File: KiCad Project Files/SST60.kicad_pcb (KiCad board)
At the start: 2 copper layers, 284.7 x 94.2 mm, 203 parts, among them J1 SM04B, J2 SWD, SW1 Boot, SW2 Reset, U1 RP2040, U2 W25Q128JVS, U3 XC6206PxxxMR, U4 PRTR5V0U2X, U5 74AHCT1G125, Y1 12MHz

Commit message: Cleaned Traces
Updated traces, generated new gerber, pos and bom, removed iso enter support
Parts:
- removed 3u Split: MX-NoLED, MX_Alps_Hybrid:MX-3U-ReversedStabilizers-NoLED (x2)
- removed D24, D29, D47, D60: D_Small, Diode_SMD:D_SOD-123
- removed the ISO at (284.2, 87.3)
- removed the ISO at (305.6, 77.8)
- removed MX77: MX-NoLED, MX_Alps_Hybrid:MX-10U-ReversedStabilizers-NoLED
- removed the Small Split at (117.5, 125.4)
- removed the Small Split at (148.4, 125.4)
- removed the Small Split at (196.1, 125.4)
- added 1.25U: MX-NoLED, MX_Alps_Hybrid:MX-1.25U-NoLED, F.Cu at (67.6, 125.5)
- added 1.25U: MX-NoLED, MX_Alps_Hybrid:MX-1.25U-NoLED, F.Cu at (91.5, 125.5)
- added 1.25U: MX-NoLED, MX_Alps_Hybrid:MX-1.25U-NoLED, F.Cu at (234.2, 125.4)
- added 1.25U: MX-NoLED, MX_Alps_Hybrid:MX-1.25U-NoLED, F.Cu at (305.7, 125.4)
- added 1.25U: MX-NoLED, MX_Alps_Hybrid:MX-1.25U-NoLED, F.Cu at (281.8, 125.4)
- added 1.25U: MX-NoLED, MX_Alps_Hybrid:MX-1.25U-NoLED, F.Cu at (43.8, 125.3)
- added 1.25U: MX-NoLED, MX_Alps_Hybrid:MX-1.25U-NoLED, F.Cu at (258.0, 125.5)
- added 2: MX-NoLED, MX_Alps_Hybrid:MX-1U-NoLED, F.Cu at (60.4, 49.2)
- added 2: MX-NoLED, MX_Alps_Hybrid:MX-1U-NoLED, F.Cu at (160.3, 106.4)
- added REF**: SW_Cherry_MX_6.25u_PCB, Button_Switch_Keyboard:SW_Cherry_MX_6.25u_PCB, F.Cu at (160.4, 130.5)
- moved D52 18.7 mm to (216.2, 127.1)
- moved D62 11.7 mm to (294.1, 128.6)
- moved D57 6.92 mm to (265.6, 127.1)
- moved D76 6.81 mm to (152.8, 119.8)
- moved D15 6.59 mm to (101.2, 122.3), turned to 180 degrees
- moved D38 5.39 mm to (183.1, 127.1)
- moved D10 4.61 mm to (77.6, 127.1)
- moved D5 4.58 mm to (53.5, 127.6)
- moved D78 4.40 mm to (192.0, 123.8)
- moved D68 3.47 mm to (308.3, 129.1)
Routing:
- net col7: track 602.4 -> 417.2 mm
- net col9: track 499.8 -> 345.7 mm
- net col5: track 438.1 -> 294.6 mm
- net col4: track 326.2 -> 238.0 mm
- net +5V: track 735.8 -> 701.5 mm
- net GND: track 140.0 -> 114.3 mm, vias 100 -> 93
- net Net-(D52-Pad2): track 4.94 -> 29.8 mm
- net Net-(D47-Pad2): track 22.5 -> 0.00 mm
- net col6: track 351.3 -> 330.4 mm
- net col1: track 97.0 -> 78.5 mm
- net Net-(D29-Pad2): track 17.8 -> 0.00 mm
- net Net-(D38-Pad2): track 4.94 -> 22.2 mm
- net Net-(D68-Pad2): track 3.98 -> 19.0 mm
- net Net-(D62-Pad2): track 4.94 -> 19.1 mm
- net Net-(D76-Pad3): track 31.4 -> 44.1 mm
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
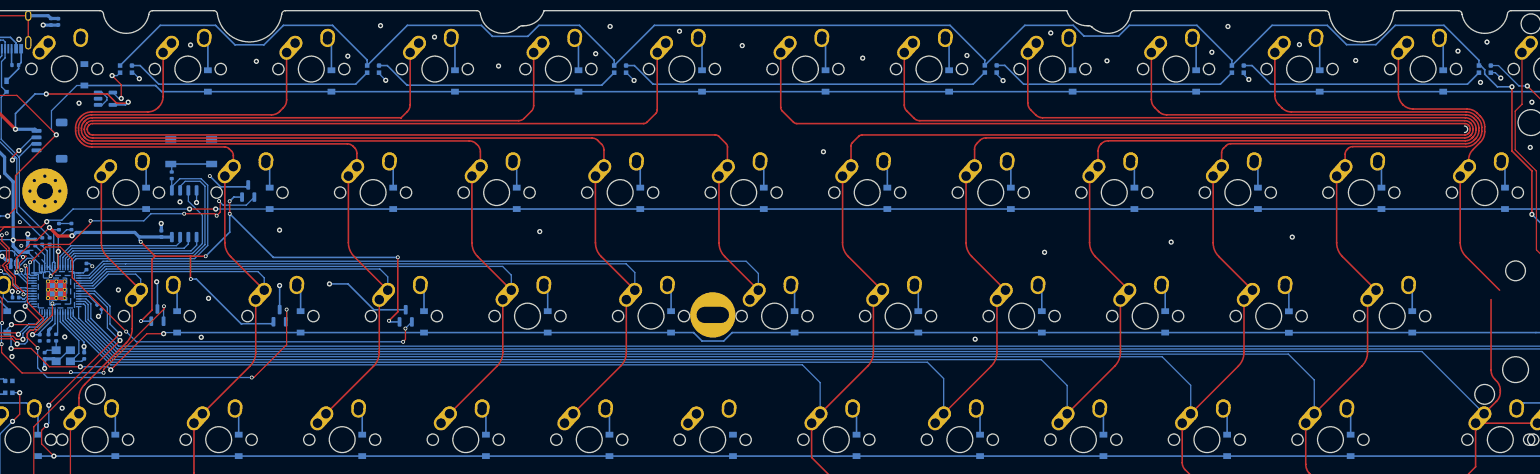
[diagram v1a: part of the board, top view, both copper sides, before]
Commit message: added traces for "c" and "1"
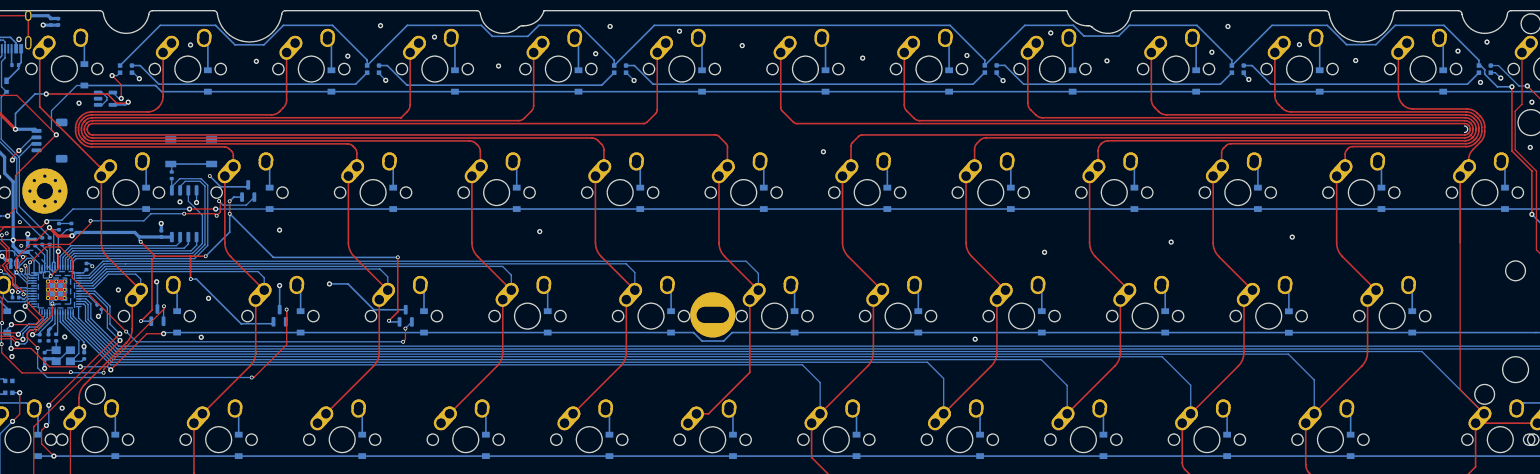
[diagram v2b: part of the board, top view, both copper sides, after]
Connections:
- 2 pad 1: (no net) -> col1
- 2 pad 2: (no net) -> Net-(D6-Pad2)
- 2 pad : (no net) -> col6
- 2 pad 1: (no net) -> col6
- 2 pad 2: (no net) -> Net-(D33-Pad2)
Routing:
- net col6: track 330.4 -> 354.5 mm
- net col1: track 78.5 -> 101.6 mm
- net col12: track 325.4 -> 335.0 mm
- net Net-(D6-Pad2): track 0.00 -> 4.00 mm
- net Net-(D33-Pad2): track 0.00 -> 3.98 mm
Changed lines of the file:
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@@
     (pad "" np_thru_hole circle (at 0 0) (size 3.9878 3.9878) (drill 3.9878) (layers "F&B.Cu" "*.Mask"))
     (pad "" np_thru_hole circle (at 5.08 0 48.0996) (size 1.75 1.75) (drill 1.75) (layers "F&B.Cu" "*.Mask"))
-    (pad "1" thru_hole oval (at -3.81 -2.54 48.0996) (size 4.211556 2.25) (drill 1.47 (offset 0.980778 0)) (layers "*.Cu" "B.Mask")
-      (pinfunction "COL") (pintype "passive"))
+    (pad "1" thru_hole oval (at -3.81 -2.54 48.099) (size 4.211556 2.25) (drill 1.47 (offset 0.980778 0)) (layers "*.Cu" "B.Mask")
+      (net 101 "col1") (pinfunction "COL") (pintype "passive"))
     (pad "1" thru_hole circle (at -2.5 -4) (size 2.25 2.25) (drill 1.47) (layers "*.Cu" "B.Mask")
-      (pinfunction "COL") (pintype "passive"))
-    (pad "2" thru_hole oval (at 2.5 -4.5 86.0548) (size 2.831378 2.25) (drill 1.47 (offset 0.290689 0)) (layers "*.Cu" "B.Mask")
-      (pinfunction "ROW") (pintype "passive"))
+      (net 101 "col1") (pinfunction "COL") (pintype "passive"))
+    (pad "2" thru_hole oval (at 2.5 -4.5 86.054) (size 2.831378 2.25) (drill 1.47 (offset 0.290689 0)) (layers "*.Cu" "B.Mask")
+      (net 16 "Net-(D6-Pad2)") (pinfunction "ROW") (pintype "passive"))
     (pad "2" thru_hole circle (at 2.54 -5.08) (size 2.25 2.25) (drill 1.47) (layers "*.Cu" "B.Mask")
-      (pinfunction "ROW") (pintype "passive"))
+      (net 16 "Net-(D6-Pad2)") (pinfunction "ROW") (pintype "passive"))
   )
   (footprint "MX_Alps_Hybrid:MX-1U-NoLED" (layer "F.Cu")
@@
       (stroke (width 0.15) (type solid)) (layer "Dwgs.User"))
     (pad "" np_thru_hole circle (at -5.08 0 48.0996) (size 1.75 1.75) (drill 1.75) (layers "F&B.Cu" "*.Mask"))
+    (pad "" thru_hole circle (at -2.5 -4) (size 2.25 2.25) (drill 1.47) (layers "*.Cu" "B.Mask")
+      (net 106 "col6") (pinfunction "COL") (pintype "passive"))
     (pad "" np_thru_hole circle (at 0 0) (size 3.9878 3.9878) (drill 3.9878) (layers "F&B.Cu" "*.Mask"))
     (pad "" np_thru_hole circle (at 5.08 0 48.0996) (size 1.75 1.75) (drill 1.75) (layers "F&B.Cu" "*.Mask"))
-    (pad "1" thru_hole oval (at -3.81 -2.54 48.0996) (size 4.211556 2.25) (drill 1.47 (offset 0.980778 0)) (layers "*.Cu" "B.Mask")
-      (pinfunction "COL") (pintype "passive"))
-    (pad "1" thru_hole circle (at -2.5 -4) (size 2.25 2.25) (drill 1.47) (layers "*.Cu" "B.Mask")
-      (pinfunction "COL") (pintype "passive"))
-    (pad "2" thru_hole oval (at 2.5 -4.5 86.0548) (size 2.831378 2.25) (drill 1.47 (offset 0.290689 0)) (layers "*.Cu" "B.Mask")
-      (pinfunction "ROW") (pintype "passive"))
+    (pad "1" thru_hole oval (at -3.81 -2.54 48.099) (size 4.211556 2.25) (drill 1.47 (offset 0.980778 0)) (layers "*.Cu" "B.Mask")
+      (net 106 "col6") (pinfunction "COL") (pintype "passive"))
+    (pad "2" thru_hole oval (at 2.5 -4.5 86.054) (size 2.831378 2.25) (drill 1.47 (offset 0.290689 0)) (layers "*.Cu" "B.Mask")
+      (net 41 "Net-(D33-Pad2)") (pinfunction "ROW") (pintype "passive"))
     (pad "2" thru_hole circle (at 2.54 -5.08) (size 2.25 2.25) (drill 1.47) (layers "*.Cu" "B.Mask")
-      (pinfunction "ROW") (pintype "passive"))
+      (net 41 "Net-(D33-Pad2)") (pinfunction "ROW") (pintype "passive"))
   )
   (footprint "MX_Alps_Hybrid:MX-1U-NoLED" (layer "F.Cu")
@@
   (segment (start 53.53 125.98) (end 53.53 124.99) (width 0.25) (layer "B.Cu") (net 15))
   (segment (start 53.53 124.99) (end 49.4525 120.9125) (width 0.25) (layer "B.Cu") (net 15))
+  (segment (start 63.425 48.45) (end 63.425 45.265) (width 0.25) (layer "B.Cu") (net 16))
+  (segment (start 63.425 45.265) (end 62.85 44.69) (width 0.25) (layer "B.Cu") (net 16))
   (segment (start 72.95 64.3625) (end 72.95 67.5) (width 0.25) (layer "B.Cu") (net 17))
   (segment (start 72.35 63.7625) (end 72.95 64.3625) (width 0.25) (layer "B.Cu") (net 17))
@@
   (segment (start 172.95 83.4) (end 172.95 86.55) (width 0.25) (layer "B.Cu") (net 40))
   (segment (start 172.3625 82.8125) (end 172.95 83.4) (width 0.25) (layer "B.Cu") (net 40))
+  (segment (start 163.45 105.6) (end 163.45 102.51) (width 0.25) (layer "B.Cu") (net 41))
+  (segment (start 163.45 102.51) (end 162.82 101.88) (width 0.25) (layer "B.Cu") (net 41))
   (segment (start 177.125 44.7125) (end 177.725 45.3125) (width 0.25) (layer "B.Cu") (net 42))
   (segment (start 177.725 45.3125) (end 177.725 49.4) (width 0.25) (layer "B.Cu") (net 42))
@@
   (segment (start 54.75 84.65) (end 54.3 85.1) (width 0.2) (layer "B.Cu") (net 100))
   (segment (start 61.2775 103.8225) (end 61.275 103.825) (width 0.2) (layer "F.Cu") (net 101))
+  (segment (start 65.75901 64.2625) (end 56.54 55.04349) (width 0.25) (layer "F.Cu") (net 101))
   (segment (start 61.275 115.3375) (end 67.35 121.4125) (width 0.2) (layer "F.Cu") (net 101))
   (segment (start 70.8025 89.279859) (end 70.8025 84.7725) (width 0.25) (layer "F.Cu") (net 101))
   (segment (start 61.275 103.825) (end 61.275 115.3375) (width 0.2) (layer "F.Cu") (net 101))
   (segment (start 66.91868 78.11868) (end 72.1125 83.3125) (width 0.25) (layer "F.Cu") (net 101))
+  (segment (start 67.35 64.2625) (end 65.75901 64.2625) (width 0.25) (layer "F.Cu") (net 101))
   (segment (start 62.5875 102.3625) (end 62.5875 99.980141) (width 0.25) (layer "F.Cu") (net 101))
+  (segment (start 56.54 55.04349) (end 56.54 46.65) (width 0.25) (layer "F.Cu") (net 101))
   (segment (start 66.04 65.7225) (end 66.04 75.997359) (width 0.25) (layer "F.Cu") (net 101))
   (segment (start 63.46618 97.85882) (end 69.92382 91.40118) (width 0.25) (layer "F.Cu") (net 101))
@@
   (segment (start 64.259964 81.45) (end 66.460444 79.24952) (width 0.2) (layer "B.Cu") (net 105))
   (segment (start 64.68566 59.375) (end 160.73934 59.375) (width 0.25) (layer "F.Cu") (net 106))
+  (segment (start 159.675807 102.38) (end 157.82 102.38) (width 0.25) (layer "F.Cu") (net 106))
   (segment (start 162.6 61.23566) (end 162.6 64.2625) (width 0.25) (layer "F.Cu") (net 106))
   (segment (start 151.765 46.6725) (end 151.765 55.52434) (width 0.25) (layer "F.Cu") (net 106))
   (segment (start 64.15533 57.84467) (end 64.09467 57.90533) (width 0.25) (layer "F.Cu") (net 106))
   (segment (start 149.66434 57.625) (end 64.68566 57.625) (width 0.25) (layer "F.Cu") (net 106))
+  (segment (start 156.51 103.84) (end 156.51 103.69) (width 0.25) (layer "F.Cu") (net 106))
   (segment (start 161.26967 59.59467) (end 162.38033 60.70533) (width 0.25) (layer "F.Cu") (net 106))
   (segment (start 162.16868 78.11868) (end 167.3625 83.3125) (width 0.25) (layer "F.Cu") (net 106))
+  (segment (start 156.51 103.69) (end 157.82 102.38) (width 0.25) (layer "F.Cu") (net 106))
+  (segment (start 166.0525 84.7725) (end 166.0525 96.003307) (width 0.25) (layer "F.Cu") (net 106))
+  (segment (start 166.0525 96.003307) (end 159.675807 102.38) (width 0.25) (layer "F.Cu") (net 106))
   (segment (start 151.54533 56.05467) (end 150.19467 57.40533) (width 0.25) (layer "F.Cu") (net 106))
   (segment (start 161.29 65.7225) (end 161.29 75.997359) (width 0.25) (layer "F.Cu") (net 106))
@@
   (segment (start 278.71455 60.471168) (end 277.559009 61.626709) (width 0.25) (layer "F.Cu") (net 112))
   (segment (start 266.065 46.6725) (end 266.065 53.083019) (width 0.25) (layer "F.Cu") (net 112))
-  (segment (start 280.3525 84.7725) (end 280.3525 95.649073) (width 0.25) (layer "F.Cu") (net 112))
   (segment (start 276.9175 121.43) (end 276.9 121.4125) (width 0.25) (layer "F.Cu") (net 112))
   (segment (start 279.3 121.43) (end 279.3 121.58) (width 0.25) (layer "F.Cu") (net 112))
-  (segment (start 281.189213 100.454537) (end 279.28125 102.3625) (width 0.25) (layer "F.Cu") (net 112))
+  (segment (start 279.28125 102.3625) (end 275.59 98.67125) (width 0.2) (layer "F.Cu") (net 112))
   (segment (start 266.72401 54.67401) (end 266.767431 54.717431) (width 0.25) (layer "F.Cu") (net 112))
   (segment (start 277.97125 103.8225) (end 287.49625 103.8225) (width 0.25) (layer "F.Cu") (net 112))
-  (segment (start 281.775 98.728427) (end 281.775 99.040323) (width 0.25) (layer "F.Cu") (net 112))
   (segment (start 277.97125 103.8225) (end 277.97125 110.55375) (width 0.25) (layer "F.Cu") (net 112))
-  (segment (start 280.938287 97.063287) (end 281.189214 97.314214) (width 0.25) (layer "F.Cu") (net 112))
   (segment (start 279.3 121.43) (end 276.9175 121.43) (width 0.25) (layer "F.Cu") (net 112))
-  (segment (start 276.46868 78.11868) (end 281.6625 83.3125) (width 0.25) (layer "F.Cu") (net 112))
+  (segment (start 275.59 98.67125) (end 275.59 65.7225) (width 0.2) (layer "F.Cu") (net 112))
   (arc (start 266.065 53.083019) (mid 266.236271 53.944057) (end 266.72401 54.67401) (width 0.25) (layer "F.Cu") (net 112))
-  (arc (start 276.46868 78.11868) (mid 275.818361 77.14541) (end 275.59 75.997359) (width 0.25) (layer "F.Cu") (net 112))
   (arc (start 276.9 63.217699) (mid 277.071271 62.356662) (end 277.559009 61.626709) (width 0.25) (layer "F.Cu") (net 112))
   (arc (start 279.37356 58.880177) (mid 279.202289 59.741215) (end 278.71455 60.471168) (width 0.25) (layer "F.Cu") (net 112))
   (arc (start 268.358421 55.37644) (mid 267.497384 55.205169) (end 266.767431 54.717431) (width 0.25) (layer "F.Cu") (net 112))
-  (arc (start 281.775 99.040323) (mid 281.622759 99.80569) (end 281.189213 100.454537) (width 0.25) (layer "F.Cu") (net 112))
-  (arc (start 280.3525 95.649073) (mid 280.504741 96.41444) (end 280.938287 97.063287) (width 0.25) (layer "F.Cu") (net 112))
   (arc (start 276.644459 55.37644) (mid 277.505497 55.547711) (end 278.23545 56.03545) (width 0.25) (layer "F.Cu") (net 112))
   (arc (start 279.37356 58.105541) (mid 279.202289 57.244504) (end 278.714551 56.514551) (width 0.25) (layer "F.Cu") (net 112))
-  (arc (start 281.775 98.728427) (mid 281.622759 97.96306) (end 281.189214 97.314214) (width 0.25) (layer "F.Cu") (net 112))
   (segment (start 269.69471 92.77596) (end 279.28125 102.3625) (width 0.2) (layer "B.Cu") (net 112))
   (segment (start 63.6 85.7) (end 63.6 88.05) (width 0.2) (layer "B.Cu") (net 112))
